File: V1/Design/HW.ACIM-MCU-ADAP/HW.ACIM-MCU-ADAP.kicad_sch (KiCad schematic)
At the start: 3 parts

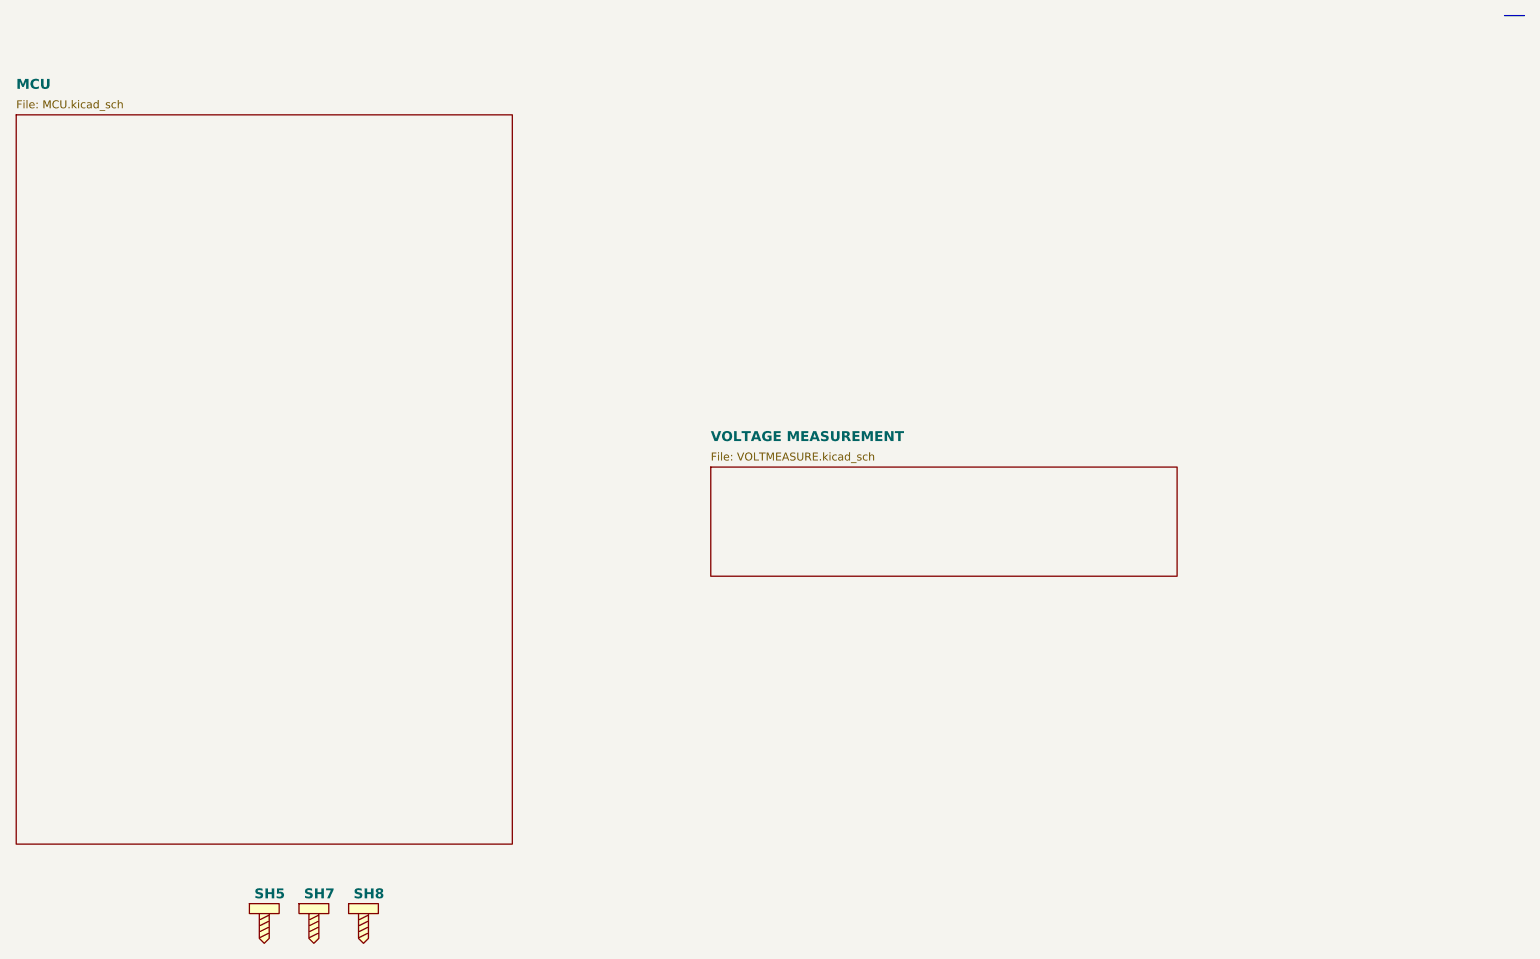
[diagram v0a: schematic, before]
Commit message: HW.ACIM-MCU-ADAP schematic update 1
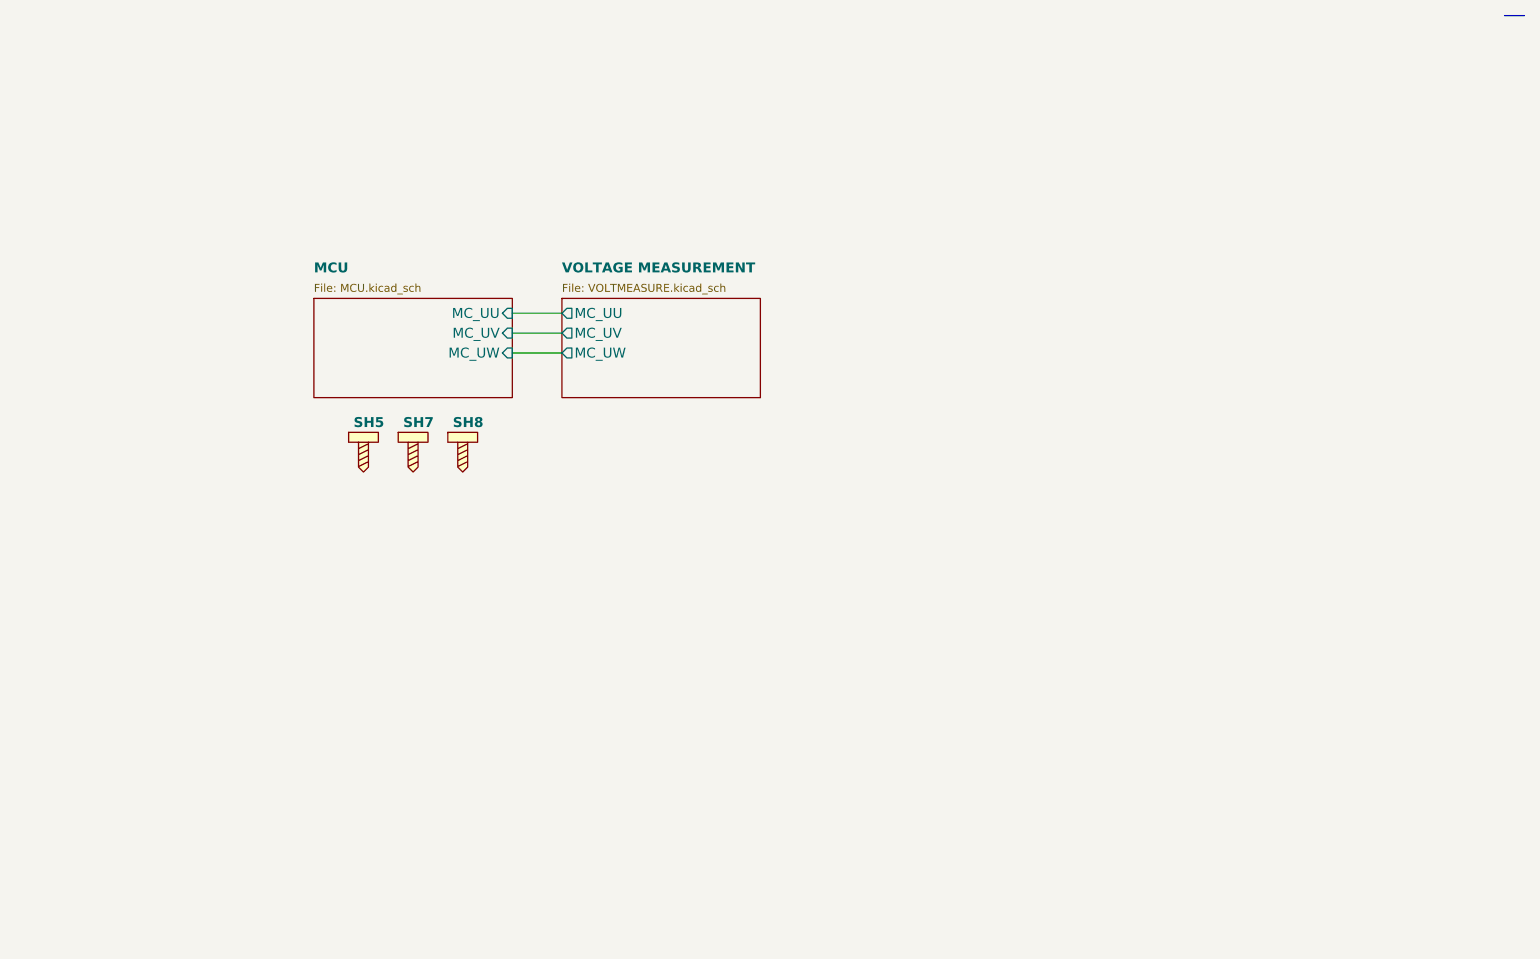
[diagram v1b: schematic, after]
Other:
- sheet MCU ports: added MC_UU, MC_UV, MC_UW; removed none
- sheet VOLTAGE MEASUREMENT ports: added MC_UU, MC_UV, MC_UW; removed none
- moved on the sheet: SH5, SH7, SH8
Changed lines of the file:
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@@
 		(rev "1.0")
+	)
+	(wire
+		(pts
+			(xy 133.35 95.885) (xy 139.7 95.885)
+		)
+		(stroke
+			(width 0)
+			(type default)
+		)
+	)
+	(wire
+		(pts
+			(xy 133.35 93.345) (xy 139.7 93.345)
+		)
+		(stroke
+			(width 0)
+			(type default)
+		)
+	)
+	(wire
+		(pts
+			(xy 133.35 90.805) (xy 139.7 90.805)
+		)
+		(stroke
+			(width 0)
+			(type default)
+		)
 	)
 	(polyline
@@
 	(symbol
 		(lib_id "SAMPI:SCREWHOLDER")
-		(at 101.6 165.1 0)
+		(at 114.3 104.775 0)
 		(unit 1)
 		(exclude_from_sim no)
@@
 		(dnp no)
 		(property "Reference" "SH5"
-			(at 100.33 165.1 0)
+			(at 113.03 104.775 0)
 			(effects
 				(font
@@
 		)
 		(property "Value" "SCREW HOLDER"
-			(at 104.14 170.1799 0)
+			(at 116.84 109.8549 0)
 			(effects
 				(font
@@
 		)
 		(property "Footprint" "SAMPI:SCREWHOLE-2.5M"
-			(at 101.6 165.1 0)
+			(at 114.3 104.775 0)
 			(effects
 				(font
@@
 		)
 		(property "Datasheet" ""
-			(at 101.6 165.1 0)
+			(at 114.3 104.775 0)
 			(effects
 				(font
@@
 		)
 		(property "Description" "PAN PHILLIPS SCREW, M2.5 X 4.5 T"
-			(at 101.6 165.1 0)
+			(at 114.3 104.775 0)
 			(effects
 				(font
@@
 		)
 		(property "MFT" "Essentra"
-			(at 101.6 165.1 0)
+			(at 114.3 104.775 0)
 			(effects
 				(font
@@
 		)
 		(property "MNP" "50M025045P012"
-			(at 101.6 165.1 0)
+			(at 114.3 104.775 0)
 			(effects
 				(font
@@
 		)
 		(property "Checked" ""
-			(at 101.6 165.1 0)
+			(at 114.3 104.775 0)
 			(effects
 				(font
@@
 		)
 		(property "Unit Price" ""
-			(at 101.6 165.1 0)
+			(at 114.3 104.775 0)
 			(effects
 				(font
@@
 	(symbol
 		(lib_id "SAMPI:SCREWHOLDER")
-		(at 107.95 165.1 0)
+		(at 120.65 104.775 0)
 		(unit 1)
 		(exclude_from_sim no)
@@
 		(dnp no)
 		(property "Reference" "SH7"
-			(at 106.68 165.1 0)
+			(at 119.38 104.775 0)
 			(effects
 				(font
@@
 		)
 		(property "Value" "SCREW HOLDER"
-			(at 110.49 170.1799 0)
+			(at 123.19 109.8549 0)
 			(effects
 				(font
@@
 		)
 		(property "Footprint" "SAMPI:SCREWHOLE-2.5M"
-			(at 107.95 165.1 0)
+			(at 120.65 104.775 0)
 			(effects
 				(font
@@
 		)
 		(property "Datasheet" ""
-			(at 107.95 165.1 0)
+			(at 120.65 104.775 0)
 			(effects
 				(font
@@
 		)
 		(property "Description" "PAN PHILLIPS SCREW, M2.5 X 4.5 T"
-			(at 107.95 165.1 0)
+			(at 120.65 104.775 0)
 			(effects
 				(font
@@
 		)
 		(property "MFT" "Essentra"
-			(at 107.95 165.1 0)
+			(at 120.65 104.775 0)
 			(effects
 				(font
@@
 		)
 		(property "MNP" "50M025045P012"
-			(at 107.95 165.1 0)
+			(at 120.65 104.775 0)
 			(effects
 				(font
@@
 		)
 		(property "Checked" ""
-			(at 107.95 165.1 0)
+			(at 120.65 104.775 0)
 			(effects
 				(font
@@
 		)
 		(property "Unit Price" ""
-			(at 107.95 165.1 0)
+			(at 120.65 104.775 0)
 			(effects
 				(font
@@
 	(symbol
 		(lib_id "SAMPI:SCREWHOLDER")
-		(at 114.3 165.1 0)
+		(at 127 104.775 0)
 		(unit 1)
 		(exclude_from_sim no)
@@
 		(dnp no)
 		(property "Reference" "SH8"
-			(at 113.03 165.1 0)
+			(at 125.73 104.775 0)
 			(effects
 				(font
@@
 		)
 		(property "Value" "SCREW HOLDER"
-			(at 116.84 170.1799 0)
+			(at 129.54 109.8549 0)
 			(effects
 				(font
@@
 		)
 		(property "Footprint" "SAMPI:SCREWHOLE-2.5M"
-			(at 114.3 165.1 0)
+			(at 127 104.775 0)
 			(effects
 				(font
@@
 		)
 		(property "Datasheet" ""
-			(at 114.3 165.1 0)
+			(at 127 104.775 0)
 			(effects
 				(font
@@
 		)
 		(property "Description" "PAN PHILLIPS SCREW, M2.5 X 4.5 T"
-			(at 114.3 165.1 0)
+			(at 127 104.775 0)
 			(effects
 				(font
@@
 		)
 		(property "MFT" "Essentra"
-			(at 114.3 165.1 0)
+			(at 127 104.775 0)
 			(effects
 				(font
@@
 		)
 		(property "MNP" "50M025045P012"
-			(at 114.3 165.1 0)
+			(at 127 104.775 0)
 			(effects
 				(font
@@
 		)
 		(property "Checked" ""
-			(at 114.3 165.1 0)
+			(at 127 104.775 0)
 			(effects
 				(font
@@
 		)
 		(property "Unit Price" ""
-			(at 114.3 165.1 0)
+			(at 127 104.775 0)
 			(effects
 				(font
@@
 	)
 	(sheet
-		(at 69.85 65.405)
-		(size 63.5 93.345)
+		(at 107.95 88.9)
+		(size 25.4 12.7)
 		(exclude_from_sim no)
 		(in_bom yes)
@@
 		)
 		(property "Sheetname" "MCU"
-			(at 69.85 62.23 0)
+			(at 107.95 85.725 0)
 			(effects
 				(font
@@
 		)
 		(property "Sheetfile" "MCU.kicad_sch"
-			(at 69.85 63.5 0)
+			(at 107.95 86.995 0)
 			(effects
 				(font
@@
 				)
 				(justify left top)
+			)
+		)
+		(pin "MC_UU" input
+			(at 133.35 90.805 0)
+			(effects
+				(font
+					(size 1.27 1.27)
+				)
+				(justify right)
+			)
+		)
+		(pin "MC_UV" input
+			(at 133.35 93.345 0)
+			(effects
+				(font
+					(size 1.27 1.27)
+				)
+				(justify right)
+			)
+		)
+		(pin "MC_UW" input
+			(at 133.35 95.885 0)
+			(effects
+				(font
+					(size 1.27 1.27)
+				)
+				(justify right)
 			)
 		)
@@
 	)
 	(sheet
-		(at 158.75 110.49)
-		(size 59.69 13.97)
+		(at 139.7 88.9)
+		(size 25.4 12.7)
 		(exclude_from_sim no)
 		(in_bom yes)
@@
 		)
 		(property "Sheetname" "VOLTAGE MEASUREMENT"
-			(at 158.75 107.315 0)
+			(at 139.7 85.725 0)
 			(effects
 				(font
@@
 		)
 		(property "Sheetfile" "VOLTMEASURE.kicad_sch"
-			(at 158.75 108.585 0)
+			(at 139.7 86.995 0)
 			(effects
 				(font
@@
 			)
 		)
+		(pin "MC_UU" output
+			(at 139.7 90.805 180)
+			(effects
+				(font
+					(size 1.27 1.27)
+				)
+				(justify left)
+			)
+		)
+		(pin "MC_UV" output
+			(at 139.7 93.345 180)
+			(effects
+				(font
+					(size 1.27 1.27)
+				)
+				(justify left)
+			)
+		)
+		(pin "MC_UW" output
+			(at 139.7 95.885 180)
+			(effects
+				(font
+					(size 1.27 1.27)
+				)
+				(justify left)
+			)
+		)
